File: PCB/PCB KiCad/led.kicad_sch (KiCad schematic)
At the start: 0 parts

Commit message: draw schematic for 60%
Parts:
- added C?: C, Capacitor_SMD:C_0805_2012Metric_Pad1.18x1.45mm_HandSolder, symbol Device:C
- added D? (x8): LED, LED_SMD:LED_1206_3216Metric_Pad1.42x1.75mm_HandSolder, symbol Device:LED
- added R? (x12): R, Resistor_SMD:R_0805_2012Metric_Pad1.20x1.40mm_HandSolder, symbol Device:R
- added U?: TLC59208FIPWR, Texas_Instruments-TLC59208FIPWR-*, symbol TLC59208:TLC59208FIPWR
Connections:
- new net: R?.1, U?.12 (~{OUT7})
- new net: D?.1 (K), R?.2 (x8)
- new net: R?.1, U?.5 (~{OUT1})
- new net: R?.2, U?.15 (SDA)
- new net: R?.1, U?.10 (~{OUT5})
- new net: R?.1, U?.11 (~{OUT6})
- new net: R?.1, R?.2, U?.13 (~{RESET})
- new net: R?.2, U?.14 (SCL)
- new net: R?.1, U?.4 (~{OUT0})
- new net: R?.1, U?.6 (~{OUT2})
- new net: R?.1, U?.7 (~{OUT3})
- new net: R?.1, U?.9 (~{OUT4})
- new net +3V3: C?.1, D?.2 (A), D?.2 (A), D?.2 (A), D?.2 (A), D?.2 (A), D?.2 (A), D?.2 (A), D?.2 (A), R?.2, U?.16 (VCC)
- new net GND: C?.2, U?.1 (A0), U?.2 (A1), U?.3 (A2), U?.8 (GND)
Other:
- note added: "TO DO: Nets Values"

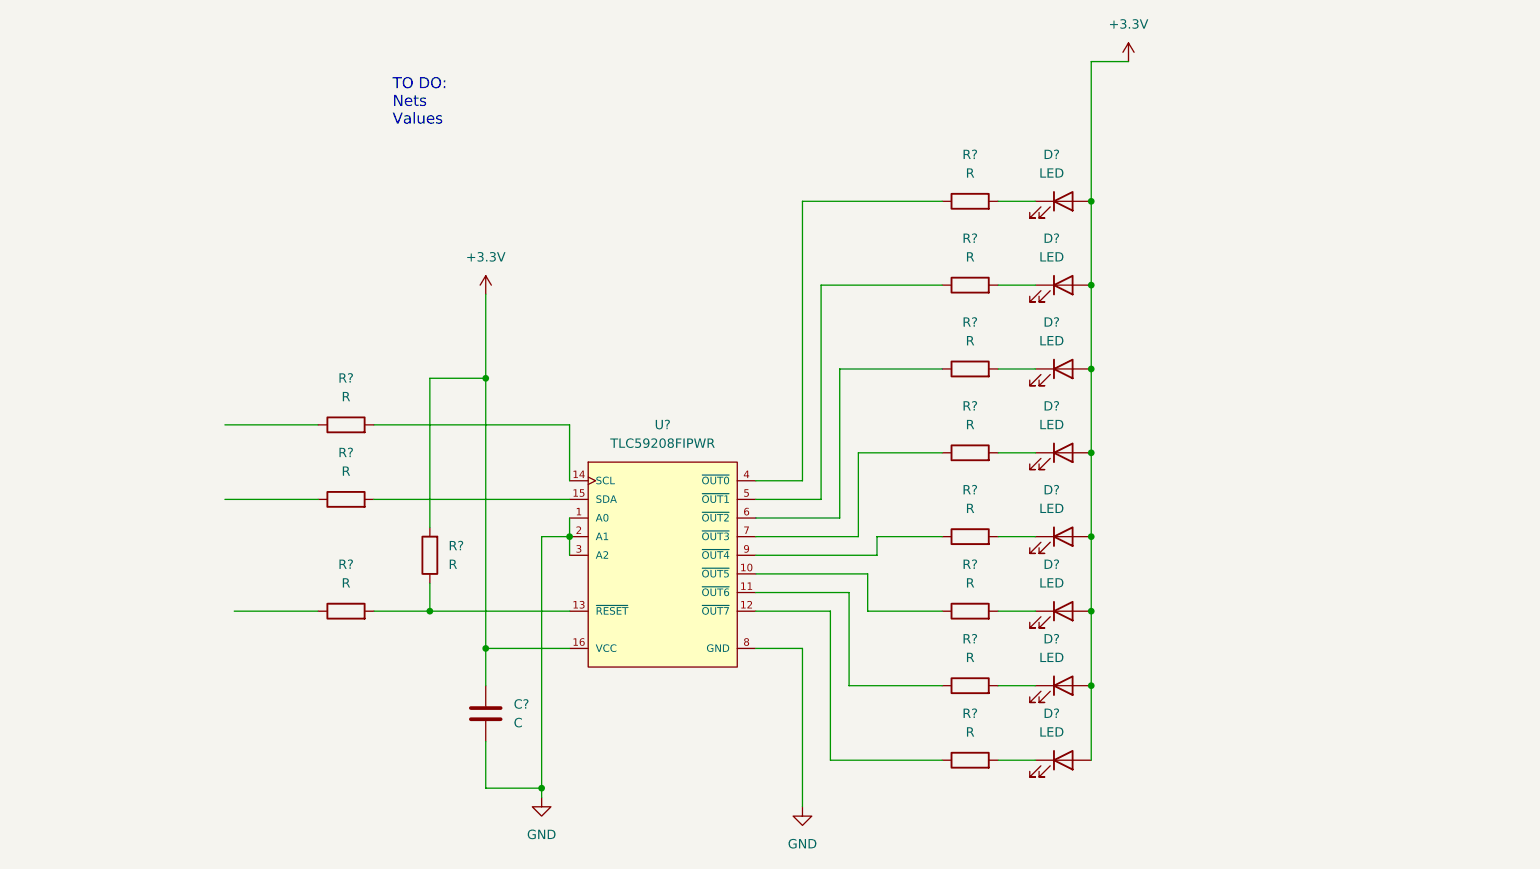
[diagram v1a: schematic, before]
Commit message: Add buttons: MCU RESET, TRIGGER
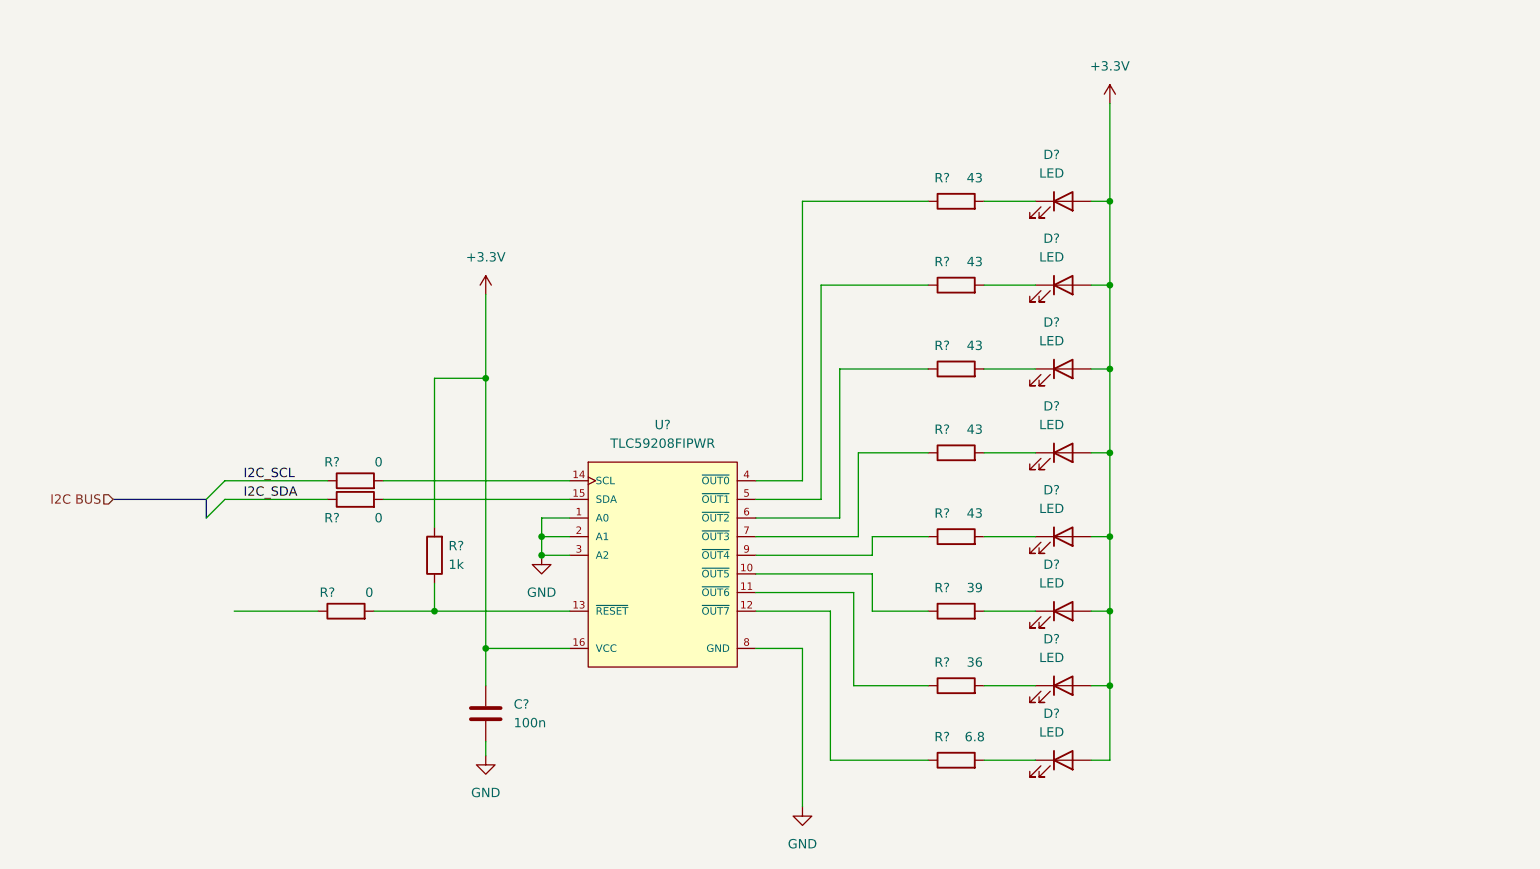
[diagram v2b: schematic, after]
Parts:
- removed R? (x7): R, Resistor_SMD:R_0805_2012Metric_Pad1.20x1.40mm_HandSolder, symbol Device:R
- added R?: 6.8, Resistor_SMD:R_0805_2012Metric_Pad1.20x1.40mm_HandSolder, symbol Device:R
- added R? (x4): 43, Resistor_SMD:R_0805_2012Metric_Pad1.20x1.40mm_HandSolder, symbol Device:R
- added R?: 39, Resistor_SMD:R_0805_2012Metric_Pad1.20x1.40mm_HandSolder, symbol Device:R
- added R?: 36, Resistor_SMD:R_0805_2012Metric_Pad1.20x1.40mm_HandSolder, symbol Device:R
- C?: value C -> 100n
- R? (x3): value R -> 0
- R?: value R -> 1k
- R?: value R -> 43
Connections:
- net at U?.12 (~{OUT7}): now also R?.1
- net at D?.1 (K): now also R?.2 (x7)
- net at U?.5 (~{OUT1}): now also R?.1
- net I2C_SDA: now reaches R?.1
- net at U?.10 (~{OUT5}): now also R?.1
- net at U?.11 (~{OUT6}): now also R?.1
- net at U?.6 (~{OUT2}): now also R?.1
- net at U?.7 (~{OUT3}): now also R?.1
- net at U?.9 (~{OUT4}): now also R?.1
- net I2C_SCL: now reaches R?.1
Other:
- note removed: "TO DO: Nets Values"
- moved on the sheet: R?

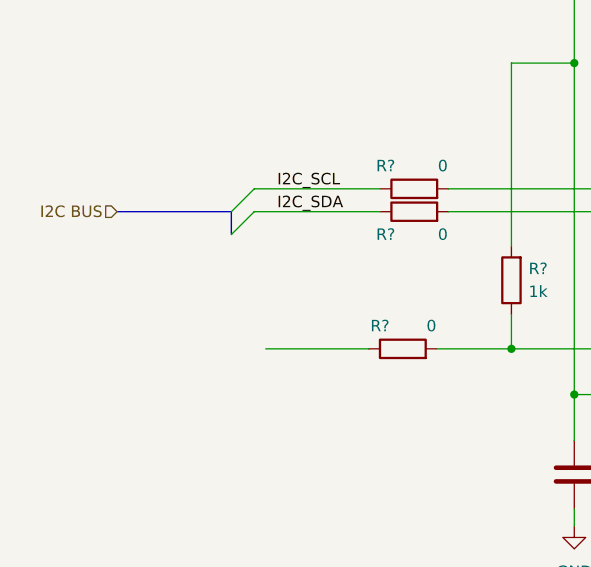
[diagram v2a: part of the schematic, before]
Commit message: Merge MCU and IO into single sheet, wire LEDs
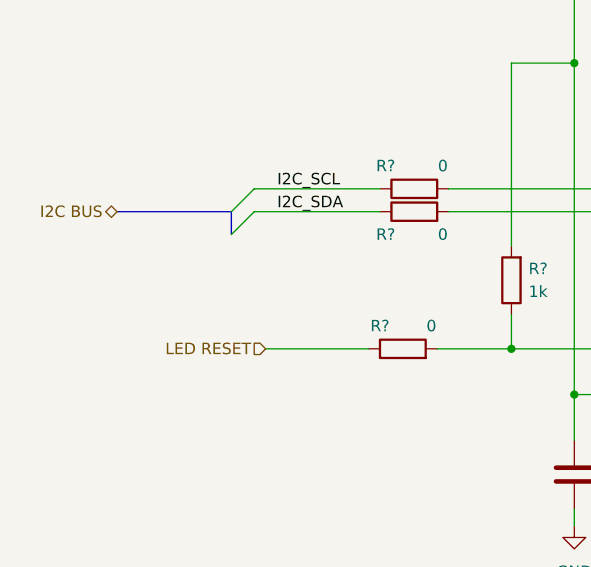
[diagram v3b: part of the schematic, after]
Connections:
- net LED RESET: now reaches R?.1
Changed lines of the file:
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@@
     (effects (font (size 1.27 1.27)) (justify left bottom))
   )
-  (hierarchical_label "I2C BUS" (shape input) (at 72.39 95.25 180)
+  (hierarchical_label "LED RESET" (shape input) (at 88.9 110.49 180)
     (effects (font (size 1.27 1.27)) (justify right))
   )
+  (hierarchical_label "I2C BUS" (shape bidirectional) (at 72.39 95.25 180)
+    (effects (font (size 1.27 1.27)) (justify right))
+  )

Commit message: first check + add connectors
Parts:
- R?: value 6.8 -> 82
- R?: value 43 -> 62
- R?: value 43 -> 56
- R?: value 39 -> 75
- R? (x2): value 43 -> 75
- R?: value 36 -> 75
- R?: value 43 -> 70
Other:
- note added: "855nm RS 173-6298 940nm RS 173-6348 1050nm digikey 11251359 nd 1200nm digikey 1125-1356-nd 1300nm digikey 1125-1335-nd 1450nm digikey 1125-1360-nd 1550nm digikey 1125-mtsm5015-194-irt-nd 1650nm digikey 1125-1362-nd"
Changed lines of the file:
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@@
     (stroke (width 0) (type default) (color 0 0 0 0))
+  )
+  (text "855nm RS 173-6298\n940nm RS 173-6348\n1050nm digikey 11251359 nd\n1200nm digikey 1125-1356-nd\n1300nm digikey 1125-1335-nd\n1450nm digikey 1125-1360-nd\n1550nm digikey 1125-mtsm5015-194-irt-nd\n1650nm digikey 1125-1362-nd"
+    (at 213.36 100.33 0)
+    (effects (font (size 1.27 1.27)) (justify left bottom))
   )
   (label "I2C_SDA" (at 90.17 95.25 0)
@@
     (in_bom yes) (on_board yes)
     (property "Reference" "R?" (id 0) (at 185.42 127.635 90))
-    (property "Value" "6.8" (id 1) (at 189.865 127.635 90))
+    (property "Value" "82" (id 1) (at 189.865 127.635 90))
     (property "Footprint" "Resistor_SMD:R_0805_2012Metric_Pad1.20x1.40mm_HandSolder" (id 2) (at 187.325 132.588 90)
       (effects (font (size 1.27 1.27)) hide)
@@
     (in_bom yes) (on_board yes)
     (property "Reference" "R?" (id 0) (at 185.42 62.865 90))
-    (property "Value" "43" (id 1) (at 189.865 62.865 90))
+    (property "Value" "62" (id 1) (at 189.865 62.865 90))
     (property "Footprint" "Resistor_SMD:R_0805_2012Metric_Pad1.20x1.40mm_HandSolder" (id 2) (at 187.325 67.818 90)
       (effects (font (size 1.27 1.27)) hide)
@@
     (in_bom yes) (on_board yes)
     (property "Reference" "R?" (id 0) (at 185.42 51.435 90))
-    (property "Value" "43" (id 1) (at 189.865 51.435 90))
+    (property "Value" "56" (id 1) (at 189.865 51.435 90))
     (property "Footprint" "Resistor_SMD:R_0805_2012Metric_Pad1.20x1.40mm_HandSolder" (id 2) (at 187.325 56.388 90)
       (effects (font (size 1.27 1.27)) hide)
@@
     (in_bom yes) (on_board yes)
     (property "Reference" "R?" (id 0) (at 185.42 107.315 90))
-    (property "Value" "39" (id 1) (at 189.865 107.315 90))
+    (property "Value" "75" (id 1) (at 189.865 107.315 90))
     (property "Footprint" "Resistor_SMD:R_0805_2012Metric_Pad1.20x1.40mm_HandSolder" (id 2) (at 187.325 112.268 90)
       (effects (font (size 1.27 1.27)) hide)
@@
     (in_bom yes) (on_board yes)
     (property "Reference" "R?" (id 0) (at 185.42 97.155 90))
-    (property "Value" "43" (id 1) (at 189.865 97.155 90))
+    (property "Value" "75" (id 1) (at 189.865 97.155 90))
     (property "Footprint" "Resistor_SMD:R_0805_2012Metric_Pad1.20x1.40mm_HandSolder" (id 2) (at 187.325 102.108 90)
       (effects (font (size 1.27 1.27)) hide)
@@
     (in_bom yes) (on_board yes)
     (property "Reference" "R?" (id 0) (at 185.42 117.475 90))
-    (property "Value" "36" (id 1) (at 189.865 117.475 90))
+    (property "Value" "75" (id 1) (at 189.865 117.475 90))
     (property "Footprint" "Resistor_SMD:R_0805_2012Metric_Pad1.20x1.40mm_HandSolder" (id 2) (at 187.325 122.428 90)
       (effects (font (size 1.27 1.27)) hide)
@@
     (in_bom yes) (on_board yes)
     (property "Reference" "R?" (id 0) (at 185.42 74.295 90))
-    (property "Value" "43" (id 1) (at 189.865 74.295 90))
+    (property "Value" "70" (id 1) (at 189.865 74.295 90))
     (property "Footprint" "Resistor_SMD:R_0805_2012Metric_Pad1.20x1.40mm_HandSolder" (id 2) (at 187.325 79.248 90)
       (effects (font (size 1.27 1.27)) hide)
@@
     (in_bom yes) (on_board yes)
     (property "Reference" "R?" (id 0) (at 185.42 85.725 90))
-    (property "Value" "43" (id 1) (at 189.865 85.725 90))
+    (property "Value" "75" (id 1) (at 189.865 85.725 90))
     (property "Footprint" "Resistor_SMD:R_0805_2012Metric_Pad1.20x1.40mm_HandSolder" (id 2) (at 187.325 90.678 90)
       (effects (font (size 1.27 1.27)) hide)

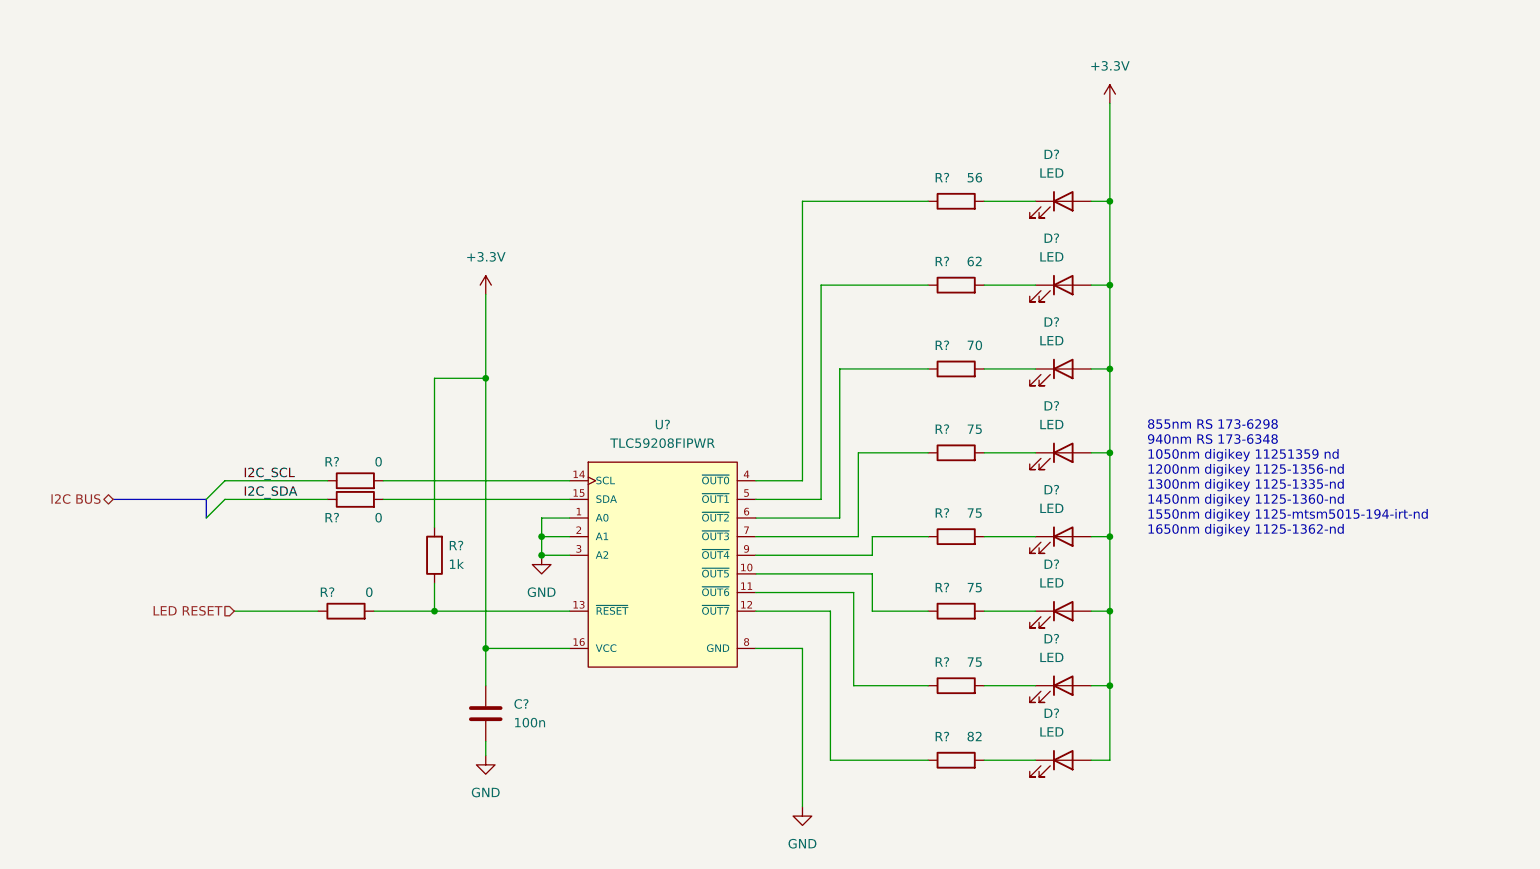
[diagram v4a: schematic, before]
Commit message: ERC: add power flags to satisfy the ERC crap
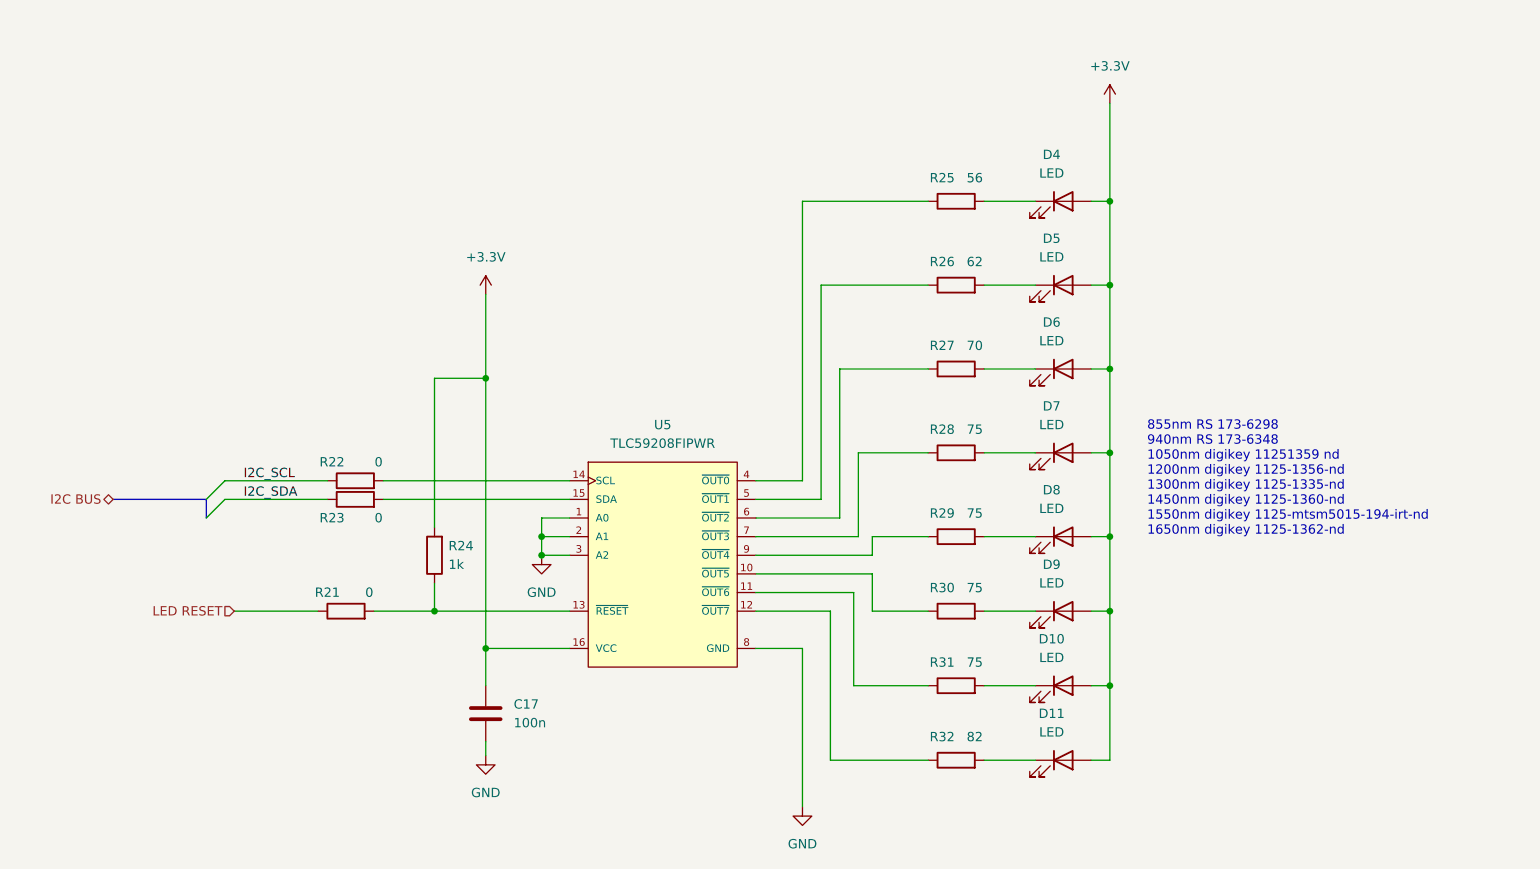
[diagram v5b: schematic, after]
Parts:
- gave numbers to parts that had none: 22

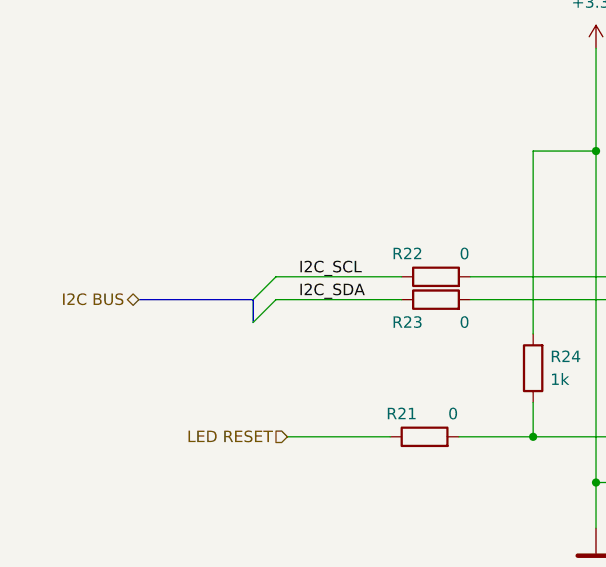
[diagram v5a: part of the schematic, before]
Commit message: Satisfy the overdemanding attention hungry ERC monster
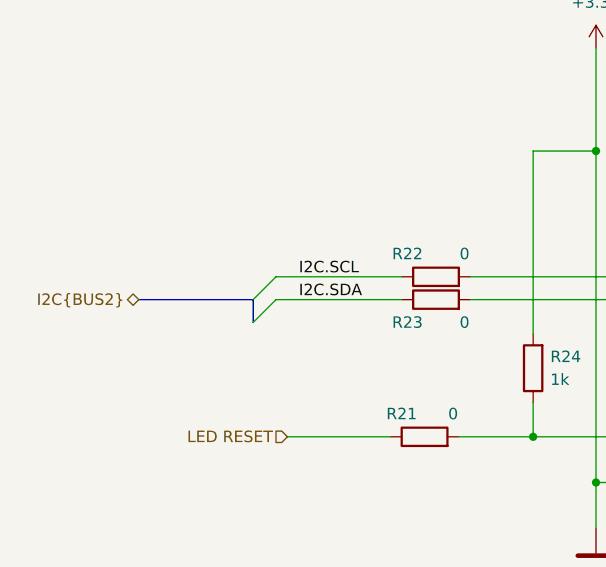
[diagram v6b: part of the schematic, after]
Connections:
- net I2C_SCL renamed I2C.SCL
- net I2C_SDA renamed I2C.SDA
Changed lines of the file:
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@@
     (effects (font (size 1.27 1.27)) (justify left bottom))
   )
-  (label "I2C_SDA" (at 90.17 95.25 0)
+  (label "I2C.SCL" (at 90.17 92.71 0)
     (effects (font (size 1.27 1.27)) (justify left bottom))
   )
-  (label "I2C_SCL" (at 90.17 92.71 0)
+  (label "I2C.SDA" (at 90.17 95.25 0)
     (effects (font (size 1.27 1.27)) (justify left bottom))
   )
@@
     (effects (font (size 1.27 1.27)) (justify right))
   )
-  (hierarchical_label "I2C BUS" (shape bidirectional) (at 72.39 95.25 180)
+  (hierarchical_label "I2C{BUS2}" (shape bidirectional) (at 72.39 95.25 180)
     (effects (font (size 1.27 1.27)) (justify right))
   )

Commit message: start of component placement
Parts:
- U5: footprint Texas_Instruments-TLC59208FIPWR-* -> TLC59208:Texas_Instruments-TLC59208FIPWR-Level_A
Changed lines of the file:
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@@
     (property "Reference" "U5" (id 0) (at 147.32 85.09 0))
     (property "Value" "TLC59208FIPWR" (id 1) (at 147.32 87.63 0))
-    (property "Footprint" "Texas_Instruments-TLC59208FIPWR-*" (id 2) (at 132.08 82.55 0)
+    (property "Footprint" "TLC59208:Texas_Instruments-TLC59208FIPWR-Level_A" (id 2) (at 132.08 82.55 0)
       (effects (font (size 1.27 1.27)) (justify left) hide)
     )
